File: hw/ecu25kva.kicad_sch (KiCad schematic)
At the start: 0 parts

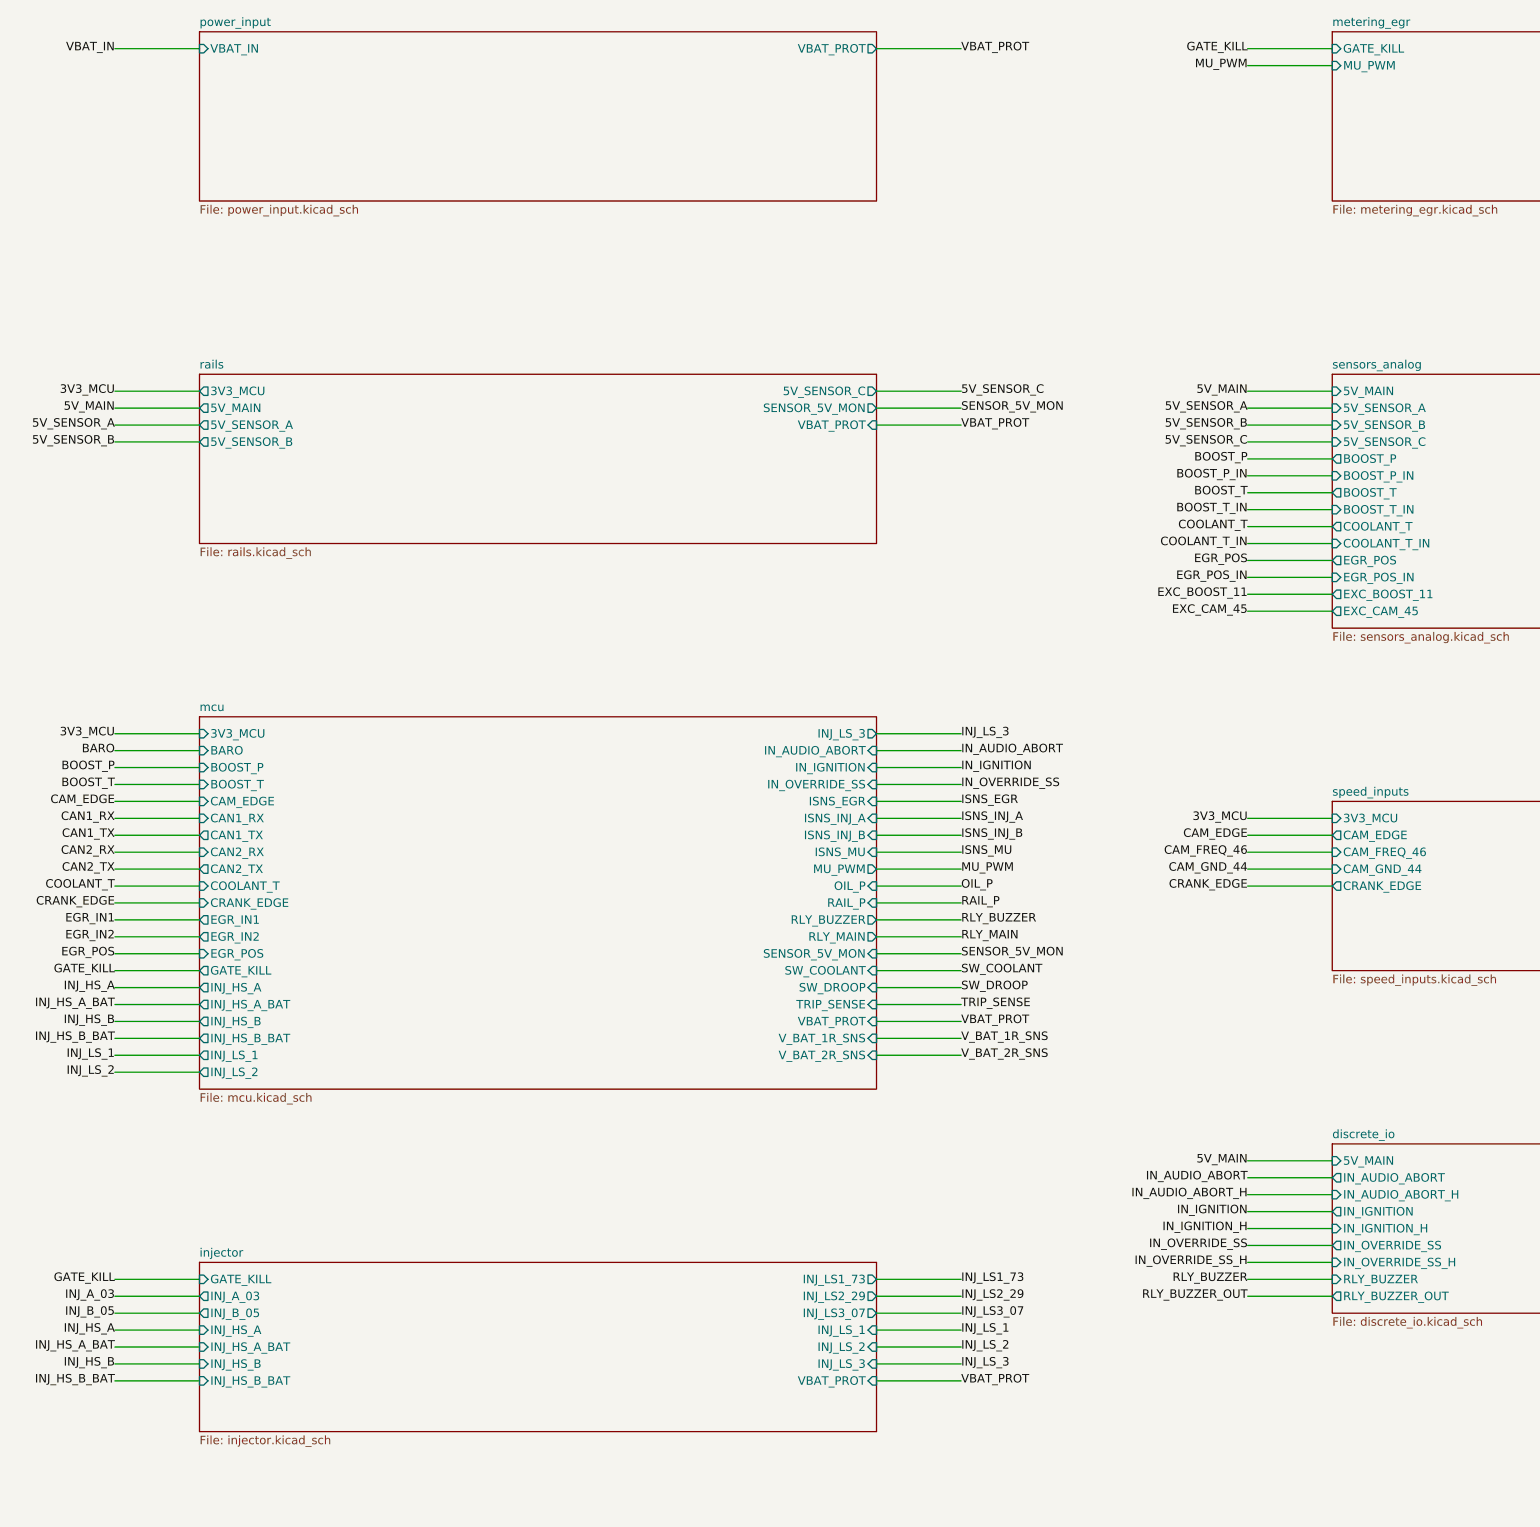
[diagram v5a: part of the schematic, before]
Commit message: Choose the gate drivers: AUIRS2181S on all eight gates, for having no interlock
Infineon AUIRS2181(4)S, datasheet retrieved and text-extracted. Its
first listed typical application is "Piezo / common rail Injection."

THE DECIDING PROPERTY IS ONE A PARAMETRIC SEARCH WOULD NEVER FILTER FOR:
no cross-conduction interlock (the datasheet's own feature table: 2181
"no", 2183/2184 "yes"). In a half bridge, HO and LO together is
shoot-through and every driver prevents it -- so the reflex is that a
driver WITHOUT interlock is the less safe choice. In an injector stage
the "high" and "low" switches are not a half bridge. They are in series
with the coil and must BOTH be on for it to conduct at all. UCC27282-Q1
and UCC27712-Q1 have interlock and could not fire an injector.

It also clears the two ratings the obvious 120 V candidate fails, and
both are now executable in run_sim.py:

  UCC27211A-Q1 HB absolute maximum 120 V, against a bank node at
  103.8 V worst case plus 12 V of VB -- 4.1 V of headroom on an
  absolute maximum. AUIRS2181S: 625 V, 5.4x.

  UCC27211A-Q1 HS DC minimum -1 V, against D_fw dropping the bank node
  1.0-1.3 V below ground on EVERY hold off-time -- violated in normal
  operation, not in a fault. AUIRS2181S operates to -5 V, clear by
  3.7 V.

Five in use: four on injector, each pairing one high side with one low
side by package rather than by circuit, and one on metering_egr for its
low side, so the board carries one gate-driver part number.

THE KILL PATH MOVES TO HIN. The part has no shutdown pin and a
ground-referenced FET cannot short a gate floating 100 V up -- but HIN
is ground-referenced, so supervisor.cir's kill FET goes there behind a
1k from the MCU. Slower than the low-side gate clamp (330 ns max driver
turn-off against 23 ns), which is acceptable because it is not the path
the fail-safe argument rests on: the low sides are in series with every
coil, and killing any one stops that cylinder.

12V_GATE, A RAIL THE BOARD DID NOT HAVE. The driv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
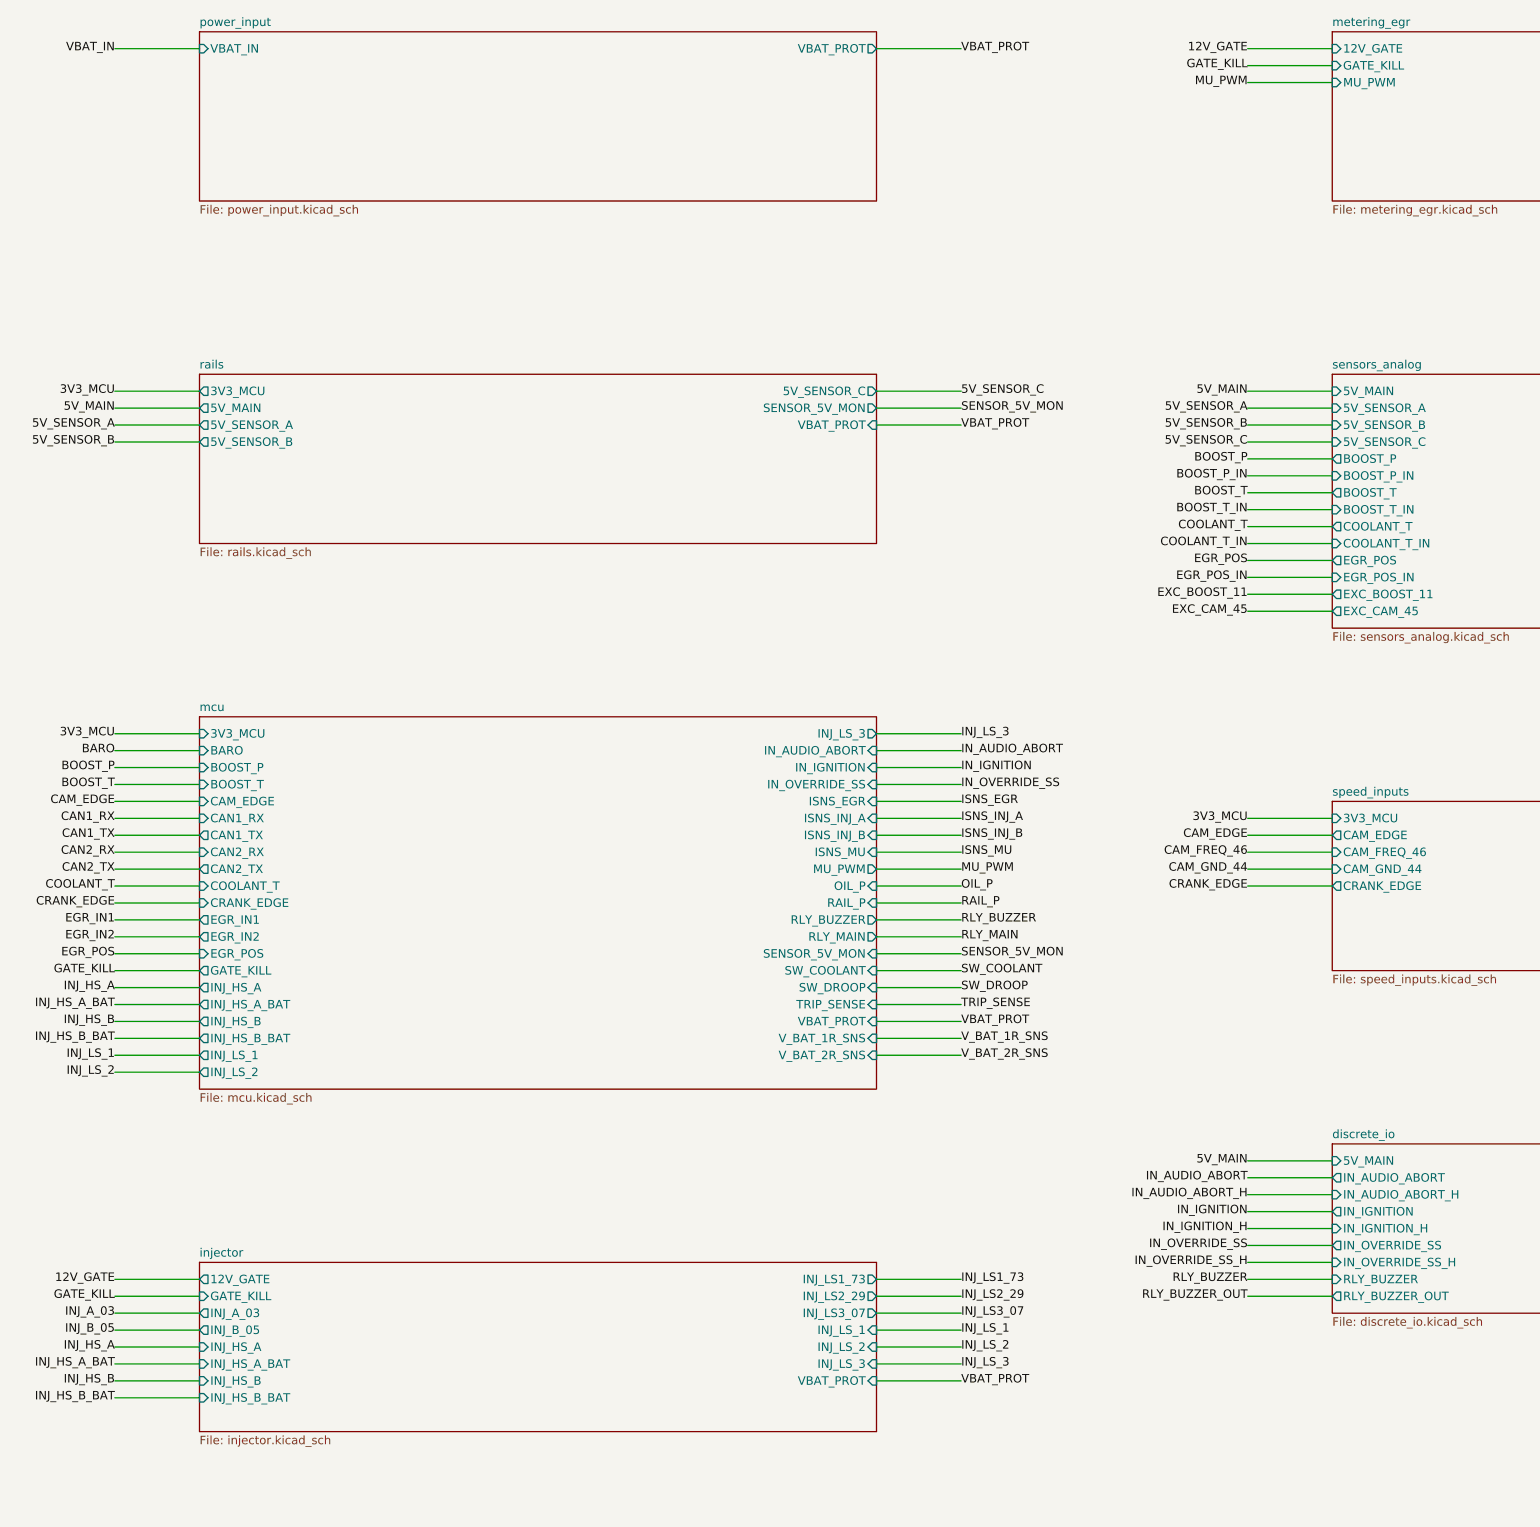
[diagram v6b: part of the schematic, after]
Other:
- sheet injector ports: added 12V_GATE; removed none
- sheet metering_egr ports: added 12V_GATE; removed none
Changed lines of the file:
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@@
       (effects (font (size 1.27 1.27)) (justify left) hide)
     )
-    (pin "GATE_KILL" input (at 45.00 215.22 180)
-      (effects (font (size 1.27 1.27)) (justify left))
-    )
-    (pin "INJ_A_03" output (at 45.00 217.76 180)
-      (effects (font (size 1.27 1.27)) (justify left))
-    )
-    (pin "INJ_B_05" output (at 45.00 220.30 180)
-      (effects (font (size 1.27 1.27)) (justify left))
-    )
-    (pin "INJ_HS_A" input (at 45.00 222.84 180)
-      (effects (font (size 1.27 1.27)) (justify left))
-    )
-    (pin "INJ_HS_A_BAT" input (at 45.00 225.38 180)
-      (effects (font (size 1.27 1.27)) (justify left))
-    )
-    (pin "INJ_HS_B" input (at 45.00 227.92 180)
-      (effects (font (size 1.27 1.27)) (justify left))
-    )
-    (pin "INJ_HS_B_BAT" input (at 45.00 230.46 180)
+    (pin "12V_GATE" output (at 45.00 215.22 180)
+      (effects (font (size 1.27 1.27)) (justify left))
+    )
+    (pin "GATE_KILL" input (at 45.00 217.76 180)
+      (effects (font (size 1.27 1.27)) (justify left))
+    )
+    (pin "INJ_A_03" output (at 45.00 220.30 180)
+      (effects (font (size 1.27 1.27)) (justify left))
+    )
+    (pin "INJ_B_05" output (at 45.00 222.84 180)
+      (effects (font (size 1.27 1.27)) (justify left))
+    )
+    (pin "INJ_HS_A" input (at 45.00 225.38 180)
+      (effects (font (size 1.27 1.27)) (justify left))
+    )
+    (pin "INJ_HS_A_BAT" input (at 45.00 227.92 180)
+      (effects (font (size 1.27 1.27)) (justify left))
+    )
+    (pin "INJ_HS_B" input (at 45.00 230.46 180)
+      (effects (font (size 1.27 1.27)) (justify left))
+    )
+    (pin "INJ_HS_B_BAT" input (at 45.00 233.00 180)
       (effects (font (size 1.27 1.27)) (justify left))
     )
@@
       (effects (font (size 1.27 1.27)) (justify left) hide)
     )
-    (pin "GATE_KILL" input (at 215.00 30.54 180)
-      (effects (font (size 1.27 1.27)) (justify left))
-    )
-    (pin "MU_PWM" input (at 215.00 33.08 180)
+    (pin "12V_GATE" input (at 215.00 30.54 180)
+      (effects (font (size 1.27 1.27)) (justify left))
+    )
+    (pin "GATE_KILL" input (at 215.00 33.08 180)
+      (effects (font (size 1.27 1.27)) (justify left))
+    )
+    (pin "MU_PWM" input (at 215.00 35.62 180)
       (effects (font (size 1.27 1.27)) (justify left))
     )
@@
     (stroke (width 0) (type default))
   )
-  (label "GATE_KILL" (at 32.30 215.22 180)
+  (label "12V_GATE" (at 32.30 215.22 180)
     (effects (font (size 1.27 1.27)) (justify right))
   )
@@
     (stroke (width 0) (type default))
   )
-  (label "INJ_A_03" (at 32.30 217.76 180)
+  (label "GATE_KILL" (at 32.30 217.76 180)
     (effects (font (size 1.27 1.27)) (justify right))
   )
@@
     (stroke (width 0) (type default))
   )
-  (label "INJ_B_05" (at 32.30 220.30 180)
+  (label "INJ_A_03" (at 32.30 220.30 180)
     (effects (font (size 1.27 1.27)) (justify right))
   )
@@
     (stroke (width 0) (type default))
   )
-  (label "INJ_HS_A" (at 32.30 222.84 180)
+  (label "INJ_B_05" (at 32.30 222.84 180)
     (effects (font (size 1.27 1.27)) (justify right))
   )
@@
     (stroke (width 0) (type default))
   )
-  (label "INJ_HS_A_BAT" (at 32.30 225.38 180)
+  (label "INJ_HS_A" (at 32.30 225.38 180)
     (effects (font (size 1.27 1.27)) (justify right))
   )
@@
     (stroke (width 0) (type default))
   )
-  (label "INJ_HS_B" (at 32.30 227.92 180)
+  (label "INJ_HS_A_BAT" (at 32.30 227.92 180)
     (effects (font (size 1.27 1.27)) (justify right))
   )
@@
     (stroke (width 0) (type default))
   )
-  (label "INJ_HS_B_BAT" (at 32.30 230.46 180)
+  (label "INJ_HS_B" (at 32.30 230.46 180)
+    (effects (font (size 1.27 1.27)) (justify right))
+  )
+  (wire (pts (xy 45.00 233.00) (xy 32.30 233.00))
+    (stroke (width 0) (type default))
+  )
+  (label "INJ_HS_B_BAT" (at 32.30 233.00 180)
     (effects (font (size 1.27 1.27)) (justify right))
   )
@@
     (stroke (width 0) (type default))
   )
-  (label "GATE_KILL" (at 202.30 30.54 180)
+  (label "12V_GATE" (at 202.30 30.54 180)
     (effects (font (size 1.27 1.27)) (justify right))
   )
@@
     (stroke (width 0) (type default))
   )
-  (label "MU_PWM" (at 202.30 33.08 180)
-    (effects (font (size 1.27 1.27)) (justify right))
-  )
+  (label "GATE_KILL" (at 202.30 33.08 180)
+    (effects (font (size 1.27 1.27)) (justify right))
+  )
+  (wire (pts (xy 215.00 35.62) (xy 202.30 35.62))
+    (stroke (width 0) (type default))
+  )
+  (label "MU_PWM" (at 202.30 35.62 180)
+    (effects (font (size 1.27 1.27)) (justify right))
+  )
